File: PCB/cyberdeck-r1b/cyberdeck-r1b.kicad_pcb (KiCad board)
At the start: 4 copper layers, 105.8 x 159.9 mm, 523 parts, among them J1 CPU_FAN, J10 DM3AT-SF-PEJM5, J11 Conn_01x22, J12 HDMI_C_1.3, J13 USB_C_Receptacle_USB2.0_16P, J15 Conn_02x20_Odd_Even, J16 1-2199119-5, J19 TSOP77438TR, J2 GP_LB, J20 Conn_01x22, J21 DX07S024JJ2R1300, J22 USB_C_Receptacle_USB2.0_16P, J3 GP_RB, J5 Conn_01x06_Pin, J6 USB_C_Receptacle_USB2.0_16P, J7 Conn_01x05, J8 PJ-342B, J9 SPK, Q1 IRLML6244, Q2 CJ2101, Q3 SI4174DY-T1-GE3_N-Channel_FET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, Q5 IRLML6244, Q6 SI4174DY-T1-GE3_N-Channel_FET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, Q7 SI4174DY-T1-GE3_N-Channel_FET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, Q8 SI4174DY-T1-GE3_N-Channel_FET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, U1 W25Q128JVS, U10 TPS62180YZFR, U11 TPS62180YZFR, U12 SY6280_OCP, U14 USBLC6-2SC6, U15 SY6280_OCP, U16 BQ76905RGRR, U17 ATtiny404-SS, U18 TPS25751SRSMR, U19 HD3SS3220IRNHT, U2 STM32F072CBT6, U20 TPD4EUSB30DQAR, U21 TPD4EUSB30DQAR, U22 AT24CS01-SSHM, U24 AT3H7B-CuH-S, U25 USBLC6-2SC6, U28 SY6280_OCP, U3 XC6206, U32 AT3H7B-CuH-S, U33 AT3H7B-CuH-S, U34 AT3H7B-CuH-S, U4 BQ25792RQMR, U5 RP2040, U6 USBLC6-2SC6, U7 CH334R, U8 PAM8406AB, U9 PCM2706CPJT, X1 X322512MSB4SI, X2 X322512MSB4SI, X3 X322512MSB4SI

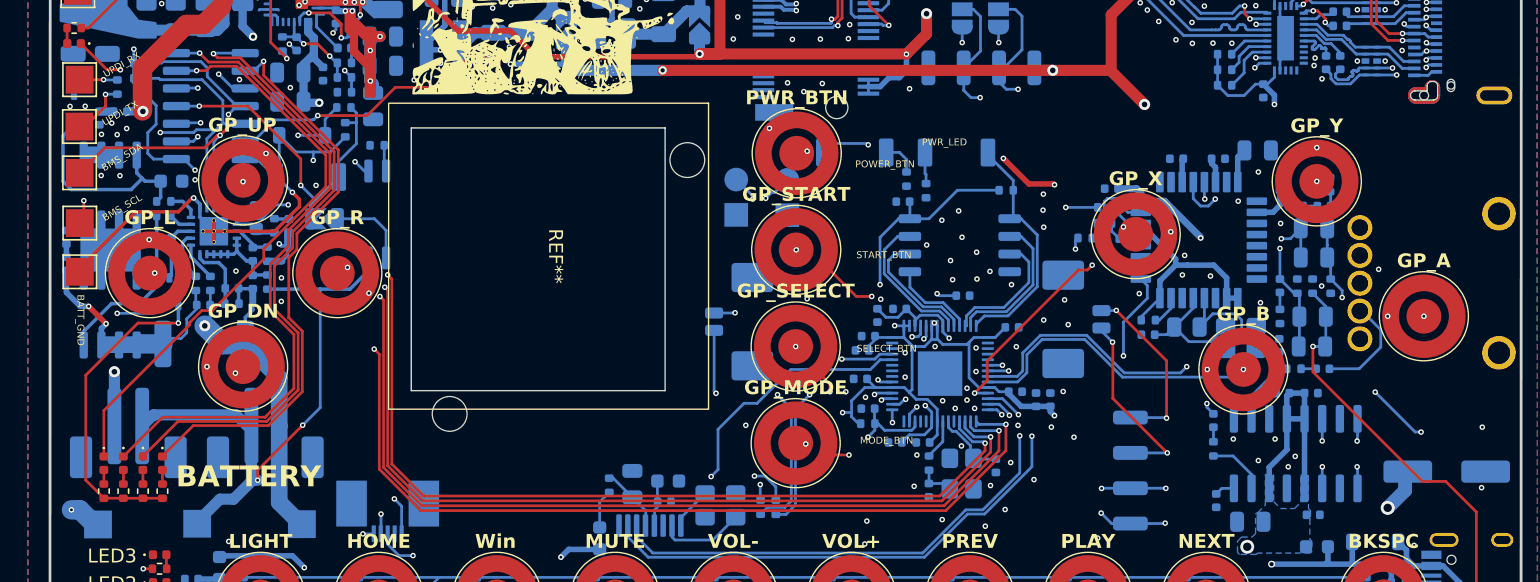
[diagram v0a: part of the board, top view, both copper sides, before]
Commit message: test usb 3 hub, test pwr regs v3
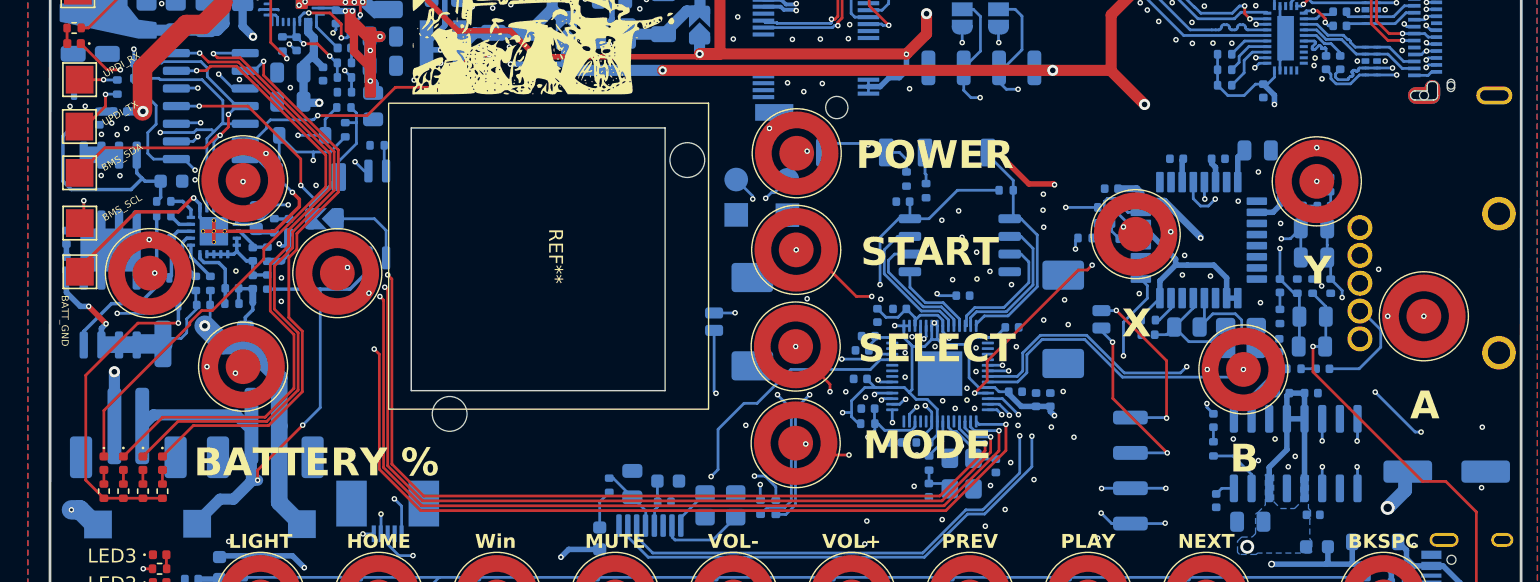
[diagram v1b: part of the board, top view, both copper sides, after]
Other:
- board text added: "BATTERY %"
- board text removed: "BATTERY"
- board text removed: "MODE_BTN"
- board text removed: "POWER_BTN"
- board text removed: "PWR_LED"
- board text removed: "SELECT_BTN"
- board text removed: "START_BTN"
